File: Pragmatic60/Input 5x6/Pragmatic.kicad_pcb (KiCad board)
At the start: 2 copper layers, 119.4 x 109.9 mm, 70 parts, among them J1 Hand-Soldering, SW1 SW_Push, SW10 SW_Push, SW11 SW_Push, SW12 SW_Push, SW13 SW_Push, SW14 SW_Push, SW15 SW_Push, SW16 SW_Push, SW17 SW_Push, SW18 SW_Push, SW19 SW_Push, SW2 SW_Push, SW20 SW_Push, SW21 SW_Push, SW22 SW_Push, SW23 SW_Push, SW24 SW_Push, SW25 SW_Push, SW26 SW_Push, SW27 SW_Push, SW28 SW_Push, SW29 SW_Push, SW3 SW_Push, SW30 SW_Push, SW4 SW_Push, SW5 SW_Push, SW6 SW_Push, SW7 SW_Push, SW8 SW_Push, SW9 SW_Push

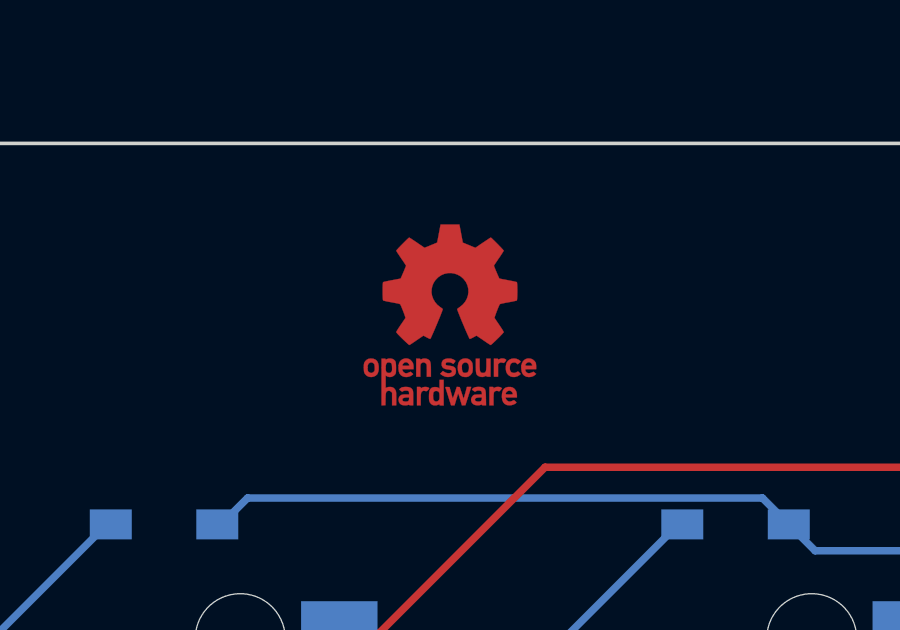
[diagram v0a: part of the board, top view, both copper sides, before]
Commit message: change logo
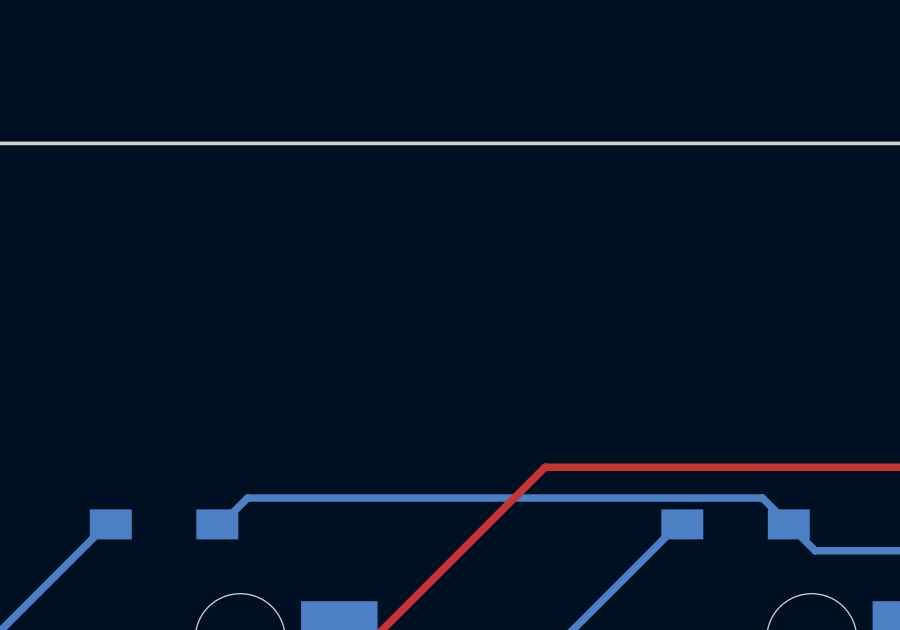
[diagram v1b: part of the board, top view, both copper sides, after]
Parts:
- removed LOGO1: Logo_Open_Hardware_Small, Symbol:OSHW-Logo_5.7x6mm_Copper
- added REF**: logo, Keyboard_JSA:Pragmatic Logo, F.Cu at (67.9, 41.3)
